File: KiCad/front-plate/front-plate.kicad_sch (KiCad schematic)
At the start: 85 parts, among them SW1 keys, SW10 keys, SW11 keys, SW12 keys, SW13 keys, SW14 keys, SW15 keys, SW16 keys, SW17 keys, SW18 keys, SW19 keys, SW2 keys, SW20 keys, SW21 keys, SW22 keys, SW23 keys, SW24 keys, SW25 keys, SW26 keys, SW27 keys, SW28 keys, SW29 keys, SW3 keys, SW30 keys, SW31 keys, SW32 keys, SW33 keys, SW34 keys, SW35 keys, SW36 keys, SW37 keys, SW38 keys, SW39 keys, SW4 keys, SW40 keys, SW41 keys, SW42 keys, SW43 keys, SW44 keys, SW45 keys, SW46 keys, SW47 keys, SW48 keys, SW49 keys, SW5 keys, SW50 keys, SW51 keys, SW52 keys, SW53 keys, SW54 keys, SW55 keys, SW56 keys, SW57 keys, SW58 keys, SW59 keys, SW6 keys, SW60 keys, SW61 keys, SW62 keys, SW63 keys, SW64 keys, SW65 keys, SW66 keys, SW67 keys, SW68 keys, SW69 keys, SW7 keys, SW70 keys, SW71 keys, SW72 keys, SW73 keys, SW74 keys, SW75 keys, SW8 keys, SW9 keys

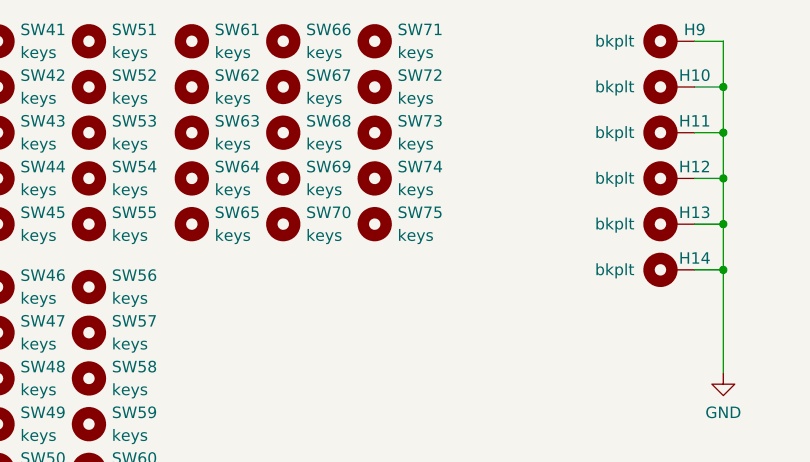
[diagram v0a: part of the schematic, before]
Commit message: front plate edge cuts
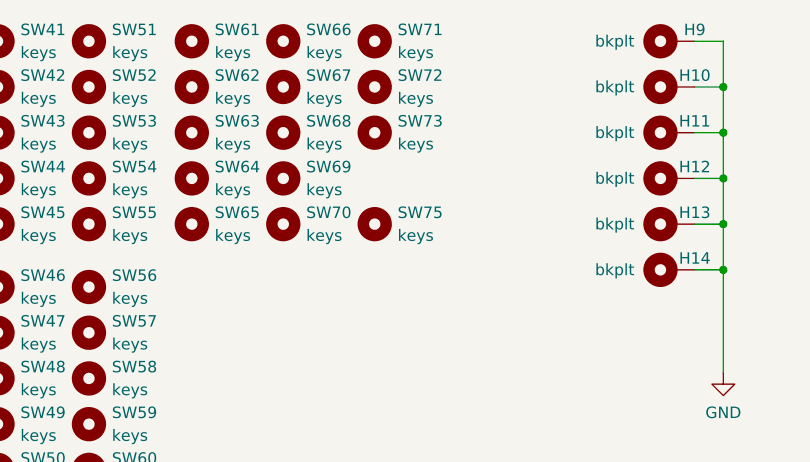
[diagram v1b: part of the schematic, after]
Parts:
- removed SW74: keys, Holes:Cherry_MX_panel_cutout, symbol Mechanical:MountingHole
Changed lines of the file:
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@@
-    )
-  )
-  (symbol (lib_id "Mechanical:MountingHole") (at 121.92 50.165 0) (unit 1)
-    (in_bom yes) (on_board yes) (fields_autoplaced)
-    (property "Reference" "SW74" (id 0) (at 124.46 48.8949 0)
-      (effects (font (size 1.27 1.27)) (justify left))
-    )
-    (property "Value" "keys" (id 1) (at 124.46 51.4349 0)
-      (effects (font (size 1.27 1.27)) (justify left))
-    )
-    (property "Footprint" "Holes:Cherry_MX_panel_cutout" (id 2) (at 121.92 50.165 0)
-      (effects (font (size 1.27 1.27)) hide)
-    )
-    (property "Datasheet" "~" (id 3) (at 121.92 50.165 0)
-      (effects (font (size 1.27 1.27)) hide)
     )
   )
@@
       (reference "SW73") (unit 1) (value "keys") (footprint "Holes:Cherry_MX_panel_cutout")
     )
-    (path "/3c8d15bc-1c4f-47d2-a610-ce614a142954"
-      (reference "SW74") (unit 1) (value "keys") (footprint "Holes:Cherry_MX_panel_cutout")
-    )
     (path "/5fa080aa-1380-49e9-91fd-900d5bf6e1fe"

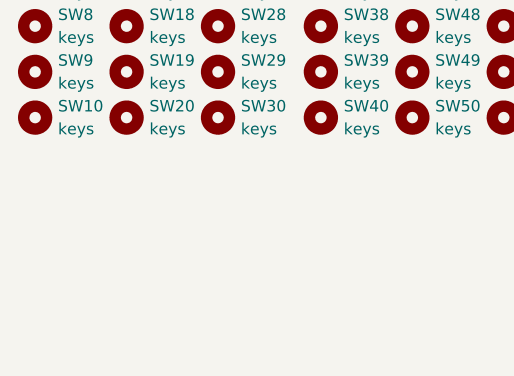
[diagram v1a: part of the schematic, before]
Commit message: LED holes
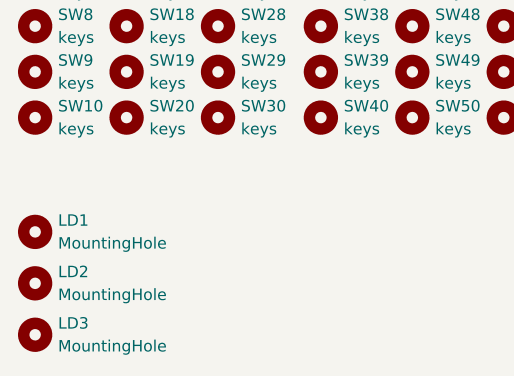
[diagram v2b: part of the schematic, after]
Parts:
- added LD1, LD2, LD3: MountingHole, MountingHole:MountingHole_4.3mm_M4, symbol Mechanical:MountingHole
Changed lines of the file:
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@@
+    )
+  )
+  (symbol (lib_id "Mechanical:MountingHole") (at 38.1 100.965 0) (unit 1)
+    (in_bom yes) (on_board yes) (fields_autoplaced)
+    (property "Reference" "LD2" (id 0) (at 40.64 99.6949 0)
+      (effects (font (size 1.27 1.27)) (justify left))
+    )
+    (property "Value" "MountingHole" (id 1) (at 40.64 102.2349 0)
+      (effects (font (size 1.27 1.27)) (justify left))
+    )
+    (property "Footprint" "MountingHole:MountingHole_4.3mm_M4" (id 2) (at 38.1 100.965 0)
+      (effects (font (size 1.27 1.27)) hide)
+    )
+    (property "Datasheet" "~" (id 3) (at 38.1 100.965 0)
+      (effects (font (size 1.27 1.27)) hide)
     )
   )
@@
     (pin "1")
   )
+  (symbol (lib_id "Mechanical:MountingHole") (at 38.1 95.25 0) (unit 1)
+    (in_bom yes) (on_board yes) (fields_autoplaced)
+    (property "Reference" "LD1" (id 0) (at 40.64 93.9799 0)
+      (effects (font (size 1.27 1.27)) (justify left))
+    )
+    (property "Value" "MountingHole" (id 1) (at 40.64 96.5199 0)
+      (effects (font (size 1.27 1.27)) (justify left))
+    )
+    (property "Footprint" "MountingHole:MountingHole_4.3mm_M4" (id 2) (at 38.1 95.25 0)
+      (effects (font (size 1.27 1.27)) hide)
+    )
+    (property "Datasheet" "~" (id 3) (at 38.1 95.25 0)
+      (effects (font (size 1.27 1.27)) hide)
+    )
+  )
   (symbol (lib_id "Mechanical:MountingHole") (at 69.85 50.165 0) (unit 1)
     (in_bom yes) (on_board yes) (fields_autoplaced)
@@
     )
   )
+  (symbol (lib_id "Mechanical:MountingHole") (at 38.1 106.68 0) (unit 1)
+    (in_bom yes) (on_board yes) (fields_autoplaced)
+    (property "Reference" "LD3" (id 0) (at 40.64 105.4099 0)
+      (effects (font (size 1.27 1.27)) (justify left))
+    )
+    (property "Value" "MountingHole" (id 1) (at 40.64 107.9499 0)
+      (effects (font (size 1.27 1.27)) (justify left))
+    )
+    (property "Footprint" "MountingHole:MountingHole_4.3mm_M4" (id 2) (at 38.1 106.68 0)
+      (effects (font (size 1.27 1.27)) hide)
+    )
+    (property "Datasheet" "~" (id 3) (at 38.1 106.68 0)
+      (effects (font (size 1.27 1.27)) hide)
+    )
+  )
   (symbol (lib_id "Mechanical:MountingHole") (at 48.26 82.55 0) (unit 1)
     (in_bom yes) (on_board yes) (fields_autoplaced)
@@
       (reference "H16") (unit 1) (value "front") (footprint "MountingHole:MountingHole_2.7mm_M2.5_DIN965_Pad")
     )
+    (path "/9e7878f6-1e16-4590-afde-f6dcdd89c22d"
+      (reference "LD1") (unit 1) (value "MountingHole") (footprint "MountingHole:MountingHole_4.3mm_M4")
+    )
+    (path "/20c594cf-c458-424d-ac08-abc63f677989"
+      (reference "LD2") (unit 1) (value "MountingHole") (footprint "MountingHole:MountingHole_4.3mm_M4")
+    )
+    (path "/eabfe1f6-e10f-4563-ae35-21fde4556042"
+      (reference "LD3") (unit 1) (value "MountingHole") (footprint "MountingHole:MountingHole_4.3mm_M4")
+    )
     (path "/6c900917-e55a-4fee-afd6-409929d528ac"

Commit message: stabilizer bar holes
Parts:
- SW21: footprint Holes:Cherry_MX_panel_cutout -> Holes:Cherry_MX_panel_cutout_spacebar
- SW68: footprint Holes:Cherry_MX_panel_cutout -> Holes:Cherry_MX_panel_cutout_2u
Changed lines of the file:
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@@
       (effects (font (size 1.27 1.27)) (justify left))
     )
-    (property "Footprint" "Holes:Cherry_MX_panel_cutout" (id 2) (at 58.42 34.925 0)
+    (property "Footprint" "Holes:Cherry_MX_panel_cutout_spacebar" (id 2) (at 58.42 34.925 0)
       (effects (font (size 1.27 1.27)) hide)
     )
@@
       (effects (font (size 1.27 1.27)) (justify left))
     )
-    (property "Footprint" "Holes:Cherry_MX_panel_cutout" (id 2) (at 111.76 45.085 0)
+    (property "Footprint" "Holes:Cherry_MX_panel_cutout_2u" (id 2) (at 111.76 45.085 0)
       (effects (font (size 1.27 1.27)) hide)
     )
@@
     )
     (path "/58dc21b6-1eac-4947-8c22-4f445a996cf7"
-      (reference "SW21") (unit 1) (value "keys") (footprint "Holes:Cherry_MX_panel_cutout")
+      (reference "SW21") (unit 1) (value "keys") (footprint "Holes:Cherry_MX_panel_cutout_spacebar")
     )
     (path "/a0f519b5-1e92-4d42-a692-38825839f615"
@@
     )
     (path "/bd4939d4-97e7-4bb4-b797-ac7a4c701563"
-      (reference "SW68") (unit 1) (value "keys") (footprint "Holes:Cherry_MX_panel_cutout")
+      (reference "SW68") (unit 1) (value "keys") (footprint "Holes:Cherry_MX_panel_cutout_2u")
     )
     (path "/14a6ec4d-b612-4c09-bc40-e2ee75de0d4a"

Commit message: Enlarge mounting holes and fix up ears templates to match main pcb
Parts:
- H10, H11, H12, H13, H14, H15, H16, H7, H8, H9: footprint MountingHole:MountingHole_2.7mm_M2.5_DIN965_Pad -> MountingHole:MountingHole_3.2mm_M3_DIN965_Pad
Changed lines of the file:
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@@
     (property "Reference" "H12" (id 0) (at 157.48 48.895 90))
     (property "Value" "bkplt" (id 1) (at 148.59 50.165 90))
-    (property "Footprint" "MountingHole:MountingHole_2.7mm_M2.5_DIN965_Pad" (id 2) (at 154.94 50.165 0)
+    (property "Footprint" "MountingHole:MountingHole_3.2mm_M3_DIN965_Pad" (id 2) (at 154.94 50.165 0)
       (effects (font (size 1.27 1.27)) hide)
     )
@@
     (property "Reference" "H11" (id 0) (at 157.48 43.815 90))
     (property "Value" "bkplt" (id 1) (at 148.59 45.085 90))
-    (property "Footprint" "MountingHole:MountingHole_2.7mm_M2.5_DIN965_Pad" (id 2) (at 154.94 45.085 0)
+    (property "Footprint" "MountingHole:MountingHole_3.2mm_M3_DIN965_Pad" (id 2) (at 154.94 45.085 0)
       (effects (font (size 1.27 1.27)) hide)
     )
@@
     (property "Reference" "H14" (id 0) (at 157.48 59.055 90))
     (property "Value" "bkplt" (id 1) (at 148.59 60.325 90))
-    (property "Footprint" "MountingHole:MountingHole_2.7mm_M2.5_DIN965_Pad" (id 2) (at 154.94 60.325 0)
+    (property "Footprint" "MountingHole:MountingHole_3.2mm_M3_DIN965_Pad" (id 2) (at 154.94 60.325 0)
       (effects (font (size 1.27 1.27)) hide)
     )
@@
     (property "Reference" "H13" (id 0) (at 157.48 53.975 90))
     (property "Value" "bkplt" (id 1) (at 148.59 55.245 90))
-    (property "Footprint" "MountingHole:MountingHole_2.7mm_M2.5_DIN965_Pad" (id 2) (at 154.94 55.245 0)
+    (property "Footprint" "MountingHole:MountingHole_3.2mm_M3_DIN965_Pad" (id 2) (at 154.94 55.245 0)
       (effects (font (size 1.27 1.27)) hide)
     )
@@
     (property "Reference" "H9" (id 0) (at 157.48 33.655 90))
     (property "Value" "bkplt" (id 1) (at 148.59 34.925 90))
-    (property "Footprint" "MountingHole:MountingHole_2.7mm_M2.5_DIN965_Pad" (id 2) (at 154.94 34.925 0)
+    (property "Footprint" "MountingHole:MountingHole_3.2mm_M3_DIN965_Pad" (id 2) (at 154.94 34.925 0)
       (effects (font (size 1.27 1.27)) hide)
     )
@@
     (property "Reference" "H10" (id 0) (at 157.48 38.735 90))
     (property "Value" "bkplt" (id 1) (at 148.59 40.005 90))
-    (property "Footprint" "MountingHole:MountingHole_2.7mm_M2.5_DIN965_Pad" (id 2) (at 154.94 40.005 0)
+    (property "Footprint" "MountingHole:MountingHole_3.2mm_M3_DIN965_Pad" (id 2) (at 154.94 40.005 0)
       (effects (font (size 1.27 1.27)) hide)
     )
@@
     (property "Reference" "H7" (id 0) (at 184.785 33.655 90))
     (property "Value" "front" (id 1) (at 175.895 34.925 90))
-    (property "Footprint" "MountingHole:MountingHole_2.7mm_M2.5_DIN965_Pad" (id 2) (at 182.245 34.925 0)
+    (property "Footprint" "MountingHole:MountingHole_3.2mm_M3_DIN965_Pad" (id 2) (at 182.245 34.925 0)
       (effects (font (size 1.27 1.27)) hide)
     )
@@
     (property "Reference" "H8" (id 0) (at 184.785 38.735 90))
     (property "Value" "front" (id 1) (at 175.895 40.005 90))
-    (property "Footprint" "MountingHole:MountingHole_2.7mm_M2.5_DIN965_Pad" (id 2) (at 182.245 40.005 0)
+    (property "Footprint" "MountingHole:MountingHole_3.2mm_M3_DIN965_Pad" (id 2) (at 182.245 40.005 0)
       (effects (font (size 1.27 1.27)) hide)
     )
@@
     (property "Reference" "H16" (id 0) (at 184.785 48.895 90))
     (property "Value" "front" (id 1) (at 175.895 50.165 90))
-    (property "Footprint" "MountingHole:MountingHole_2.7mm_M2.5_DIN965_Pad" (id 2) (at 182.245 50.165 0)
+    (property "Footprint" "MountingHole:MountingHole_3.2mm_M3_DIN965_Pad" (id 2) (at 182.245 50.165 0)
       (effects (font (size 1.27 1.27)) hide)
     )
@@
     (property "Reference" "H15" (id 0) (at 184.785 43.815 90))
     (property "Value" "front" (id 1) (at 175.895 45.085 90))
-    (property "Footprint" "MountingHole:MountingHole_2.7mm_M2.5_DIN965_Pad" (id 2) (at 182.245 45.085 0)
+    (property "Footprint" "MountingHole:MountingHole_3.2mm_M3_DIN965_Pad" (id 2) (at 182.245 45.085 0)
       (effects (font (size 1.27 1.27)) hide)
     )
@@
     )
     (path "/9d8b977a-8f1c-4921-8389-104009d83dee"
-      (reference "H7") (unit 1) (value "front") (footprint "MountingHole:MountingHole_2.7mm_M2.5_DIN965_Pad")
+      (reference "H7") (unit 1) (value "front") (footprint "MountingHole:MountingHole_3.2mm_M3_DIN965_Pad")
     )
     (path "/c01d7d2f-3610-4875-ac5c-775e83d33258"
-      (reference "H8") (unit 1) (value "front") (footprint "MountingHole:MountingHole_2.7mm_M2.5_DIN965_Pad")
+      (reference "H8") (unit 1) (value "front") (footprint "MountingHole:MountingHole_3.2mm_M3_DIN965_Pad")
     )
     (path "/7a0ae22c-83e6-45e4-a6d1-db6245854e5d"
-      (reference "H9") (unit 1) (value "bkplt") (footprint "MountingHole:MountingHole_2.7mm_M2.5_DIN965_Pad")
+      (reference "H9") (unit 1) (value "bkplt") (footprint "MountingHole:MountingHole_3.2mm_M3_DIN965_Pad")
     )
     (path "/82c7eec0-d68a-4d30-9eb0-8b69ef275f47"
-      (reference "H10") (unit 1) (value "bkplt") (footprint "MountingHole:MountingHole_2.7mm_M2.5_DIN965_Pad")
+      (reference "H10") (unit 1) (value "bkplt") (footprint "MountingHole:MountingHole_3.2mm_M3_DIN965_Pad")
     )
     (path "/30d2eb3d-ee9e-44ce-86e0-1487ae0c798a"
-      (reference "H11") (unit 1) (value "bkplt") (footprint "MountingHole:MountingHole_2.7mm_M2.5_DIN965_Pad")
+      (reference "H11") (unit 1) (value "bkplt") (footprint "MountingHole:MountingHole_3.2mm_M3_DIN965_Pad")
     )
     (path "/11fddb54-25b7-47c8-b281-9a14ba172339"
-      (reference "H12") (unit 1) (value "bkplt") (footprint "MountingHole:MountingHole_2.7mm_M2.5_DIN965_Pad")
+      (reference "H12") (unit 1) (value "bkplt") (footprint "MountingHole:MountingHole_3.2mm_M3_DIN965_Pad")
     )
     (path "/4677916f-2a64-4dc9-979e-355588a0b7a3"
-      (reference "H13") (unit 1) (value "bkplt") (footprint "MountingHole:MountingHole_2.7mm_M2.5_DIN965_Pad")
+      (reference "H13") (unit 1) (value "bkplt") (footprint "MountingHole:MountingHole_3.2mm_M3_DIN965_Pad")
     )
     (path "/399d9881-e3d8-40e5-96cb-7180cf53750f"
-      (reference "H14") (unit 1) (value "bkplt") (footprint "MountingHole:MountingHole_2.7mm_M2.5_DIN965_Pad")
+      (reference "H14") (unit 1) (value "bkplt") (footprint "MountingHole:MountingHole_3.2mm_M3_DIN965_Pad")
     )
     (path "/efffe9ca-f880-4c84-8b54-b63bdef4a123"
-      (reference "H15") (unit 1) (value "front") (footprint "MountingHole:MountingHole_2.7mm_M2.5_DIN965_Pad")
+      (reference "H15") (unit 1) (value "front") (footprint "MountingHole:MountingHole_3.2mm_M3_DIN965_Pad")
     )
     (path "/c425bfc5-95d3-420b-a3d0-f112428417ec"
-      (reference "H16") (unit 1) (value "front") (footprint "MountingHole:MountingHole_2.7mm_M2.5_DIN965_Pad")
+      (reference "H16") (unit 1) (value "front") (footprint "MountingHole:MountingHole_3.2mm_M3_DIN965_Pad")
     )
     (path "/9e7878f6-1e16-4590-afde-f6dcdd89c22d"

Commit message: larger LED holes, remove silkscreen designators
update LED holes in schematic

larger LED holes, remove silkscreens
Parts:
- LD1, LD2, LD3: footprint MountingHole:MountingHole_4.3mm_M4 -> MountingHole:MountingHole_5.5mm
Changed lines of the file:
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@@
       (effects (font (size 1.27 1.27)) (justify left))
     )
-    (property "Footprint" "MountingHole:MountingHole_4.3mm_M4" (id 2) (at 38.1 100.965 0)
+    (property "Footprint" "MountingHole:MountingHole_5.5mm" (id 2) (at 38.1 100.965 0)
       (effects (font (size 1.27 1.27)) hide)
     )
@@
       (effects (font (size 1.27 1.27)) (justify left))
     )
-    (property "Footprint" "MountingHole:MountingHole_4.3mm_M4" (id 2) (at 38.1 95.25 0)
+    (property "Footprint" "MountingHole:MountingHole_5.5mm" (id 2) (at 38.1 95.25 0)
       (effects (font (size 1.27 1.27)) hide)
     )
@@
       (effects (font (size 1.27 1.27)) (justify left))
     )
-    (property "Footprint" "MountingHole:MountingHole_4.3mm_M4" (id 2) (at 38.1 106.68 0)
+    (property "Footprint" "MountingHole:MountingHole_5.5mm" (id 2) (at 38.1 106.68 0)
       (effects (font (size 1.27 1.27)) hide)
     )
@@
     )
     (path "/9e7878f6-1e16-4590-afde-f6dcdd89c22d"
-      (reference "LD1") (unit 1) (value "MountingHole") (footprint "MountingHole:MountingHole_4.3mm_M4")
+      (reference "LD1") (unit 1) (value "MountingHole") (footprint "MountingHole:MountingHole_5.5mm")
     )
     (path "/20c594cf-c458-424d-ac08-abc63f677989"
-      (reference "LD2") (unit 1) (value "MountingHole") (footprint "MountingHole:MountingHole_4.3mm_M4")
+      (reference "LD2") (unit 1) (value "MountingHole") (footprint "MountingHole:MountingHole_5.5mm")
     )
     (path "/eabfe1f6-e10f-4563-ae35-21fde4556042"
-      (reference "LD3") (unit 1) (value "MountingHole") (footprint "MountingHole:MountingHole_4.3mm_M4")
+      (reference "LD3") (unit 1) (value "MountingHole") (footprint "MountingHole:MountingHole_5.5mm")
     )
     (path "/6c900917-e55a-4fee-afd6-409929d528ac"
